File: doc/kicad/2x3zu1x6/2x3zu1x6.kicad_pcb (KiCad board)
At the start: 2 copper layers, 25.4 x 30.5 mm, 2 parts, among them J1 Conn_01x06_Male, J2 Conn_02x03_Top_Bottom

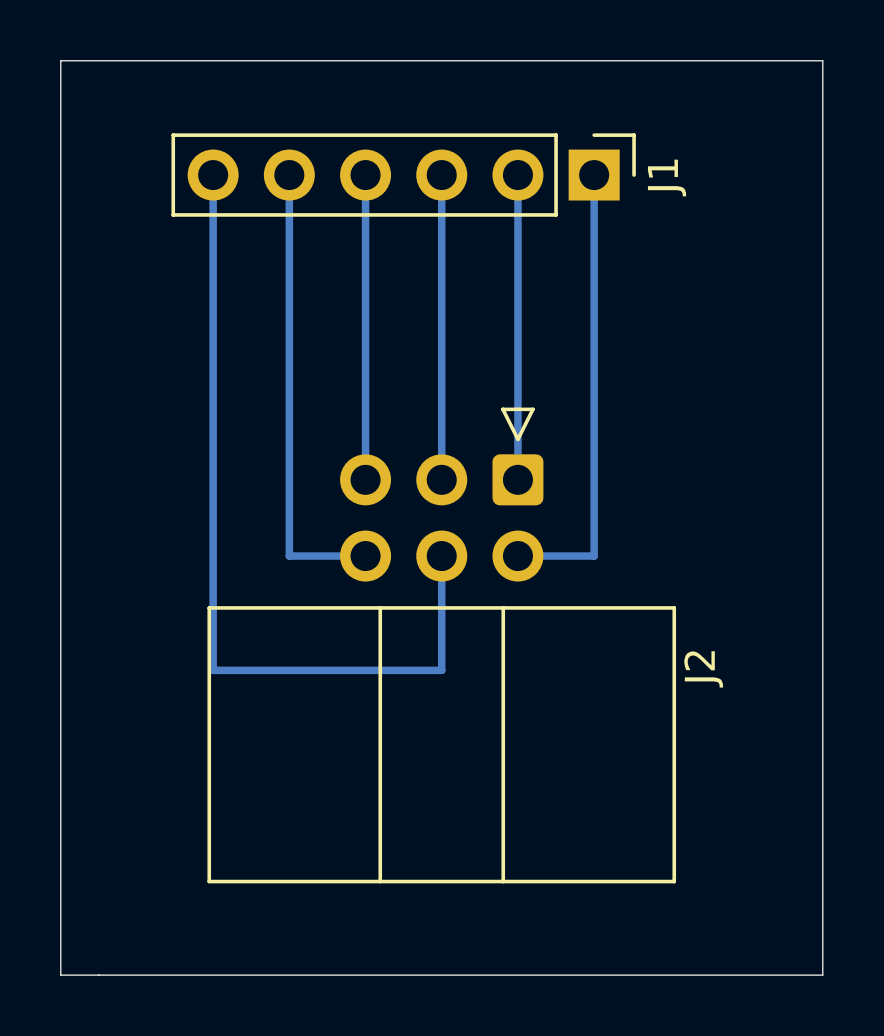
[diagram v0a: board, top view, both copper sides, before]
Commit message: Ecken rund gemacht, alle mit Montagelöcher
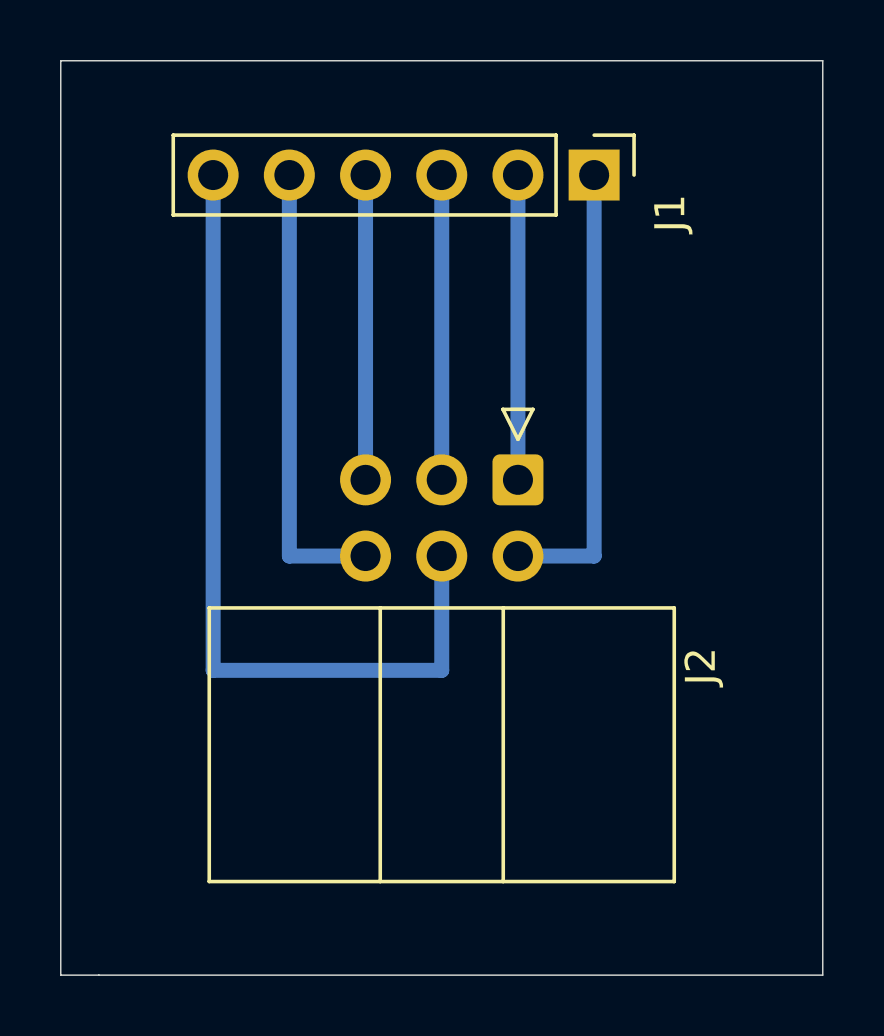
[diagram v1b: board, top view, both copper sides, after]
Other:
- net class Default: trace_width 0.25 -> 0.5

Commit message: Platinen, die an jlcpcb geschickt worden sind.
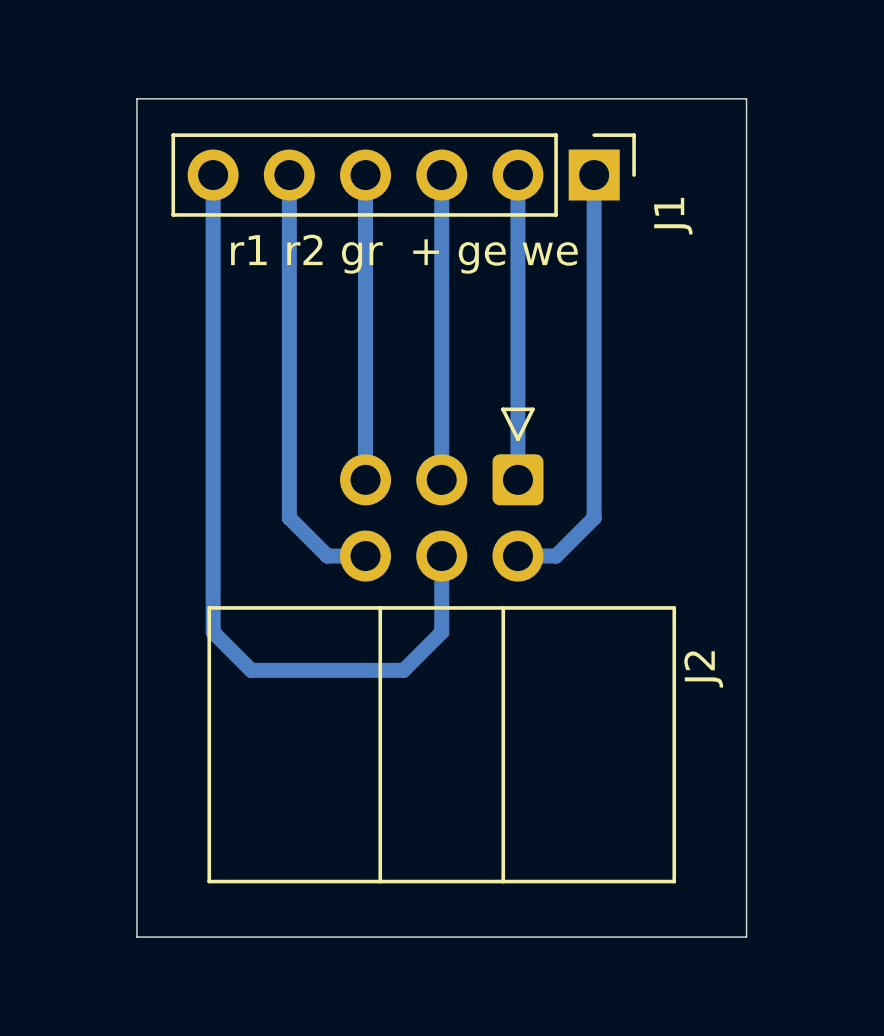
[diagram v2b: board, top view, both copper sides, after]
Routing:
- net Net-(J1-Pad6): track 27.9 -> 26.5 mm
- net Net-(J1-Pad5): track 15.2 -> 14.5 mm
- net Net-(J1-Pad1): track 15.2 -> 14.5 mm
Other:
- board size 25.4 x 30.5 mm -> 20.3 x 27.9 mm
- board text added: "r1 r2 gr + ge we"

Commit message: Alte Datei gelöscht, 6er-Dateien hinzugefügt
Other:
- net class Default removed
